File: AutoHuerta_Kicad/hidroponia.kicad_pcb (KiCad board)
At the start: 2 copper layers, 37 parts, among them J1 bornera, J2 bornera, J3 Barrel_Jack, J4 pin, J6 Pin, J7 Pin, K1 RELAY, Q1 BC817, Q2 BS170F, Q3 BC817, U2 PC817, U3 L7805, U4 PC817, U5 L7805, U6 PC817

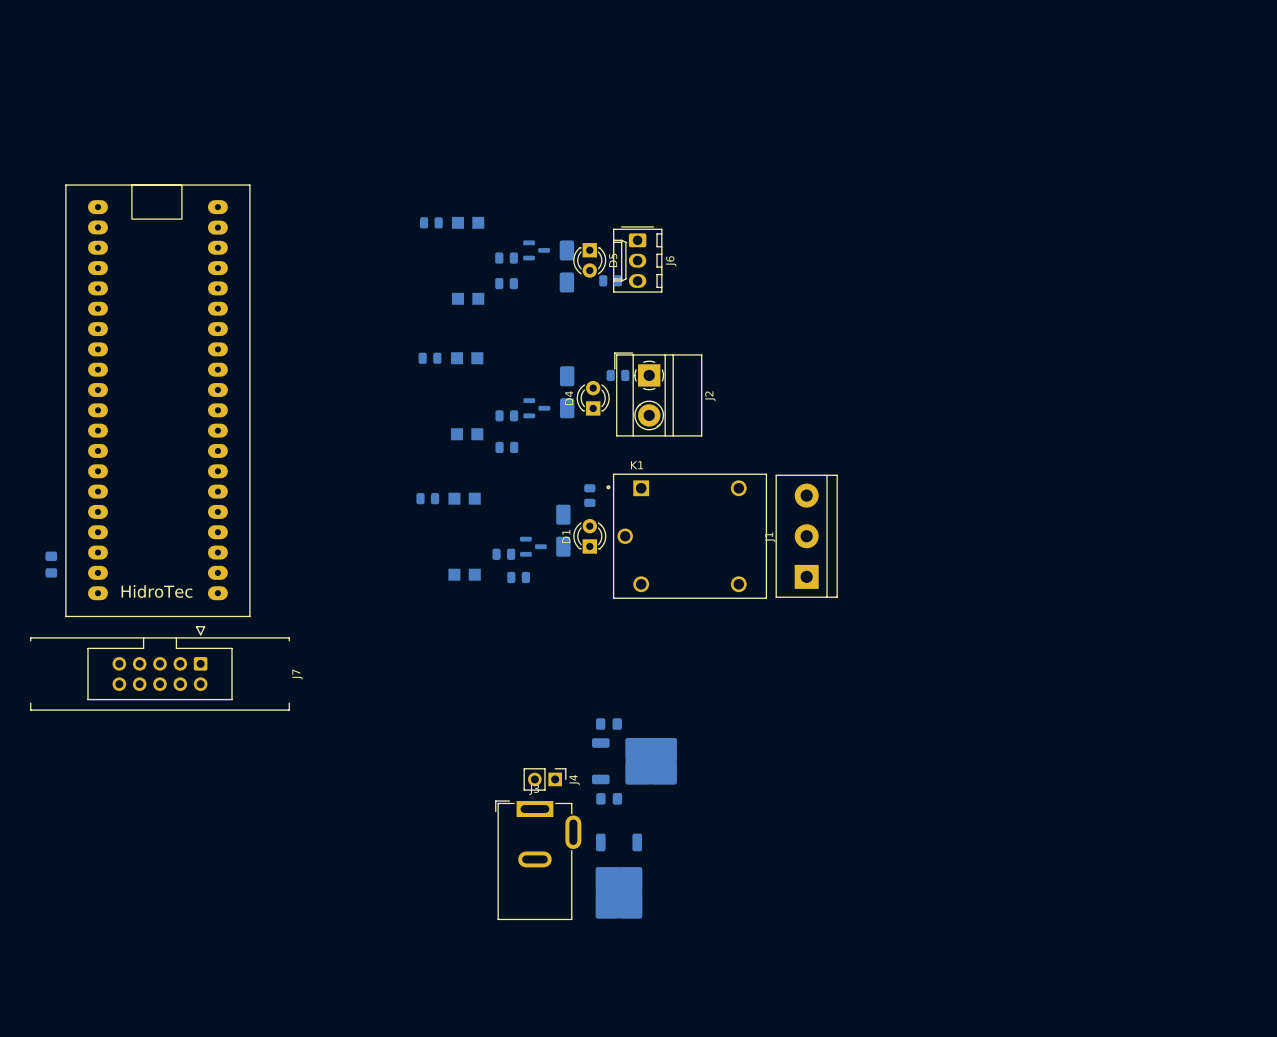
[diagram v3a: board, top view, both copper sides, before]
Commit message: PCB
PCB casi terminado, y cambiamos unas cosas del esquematico
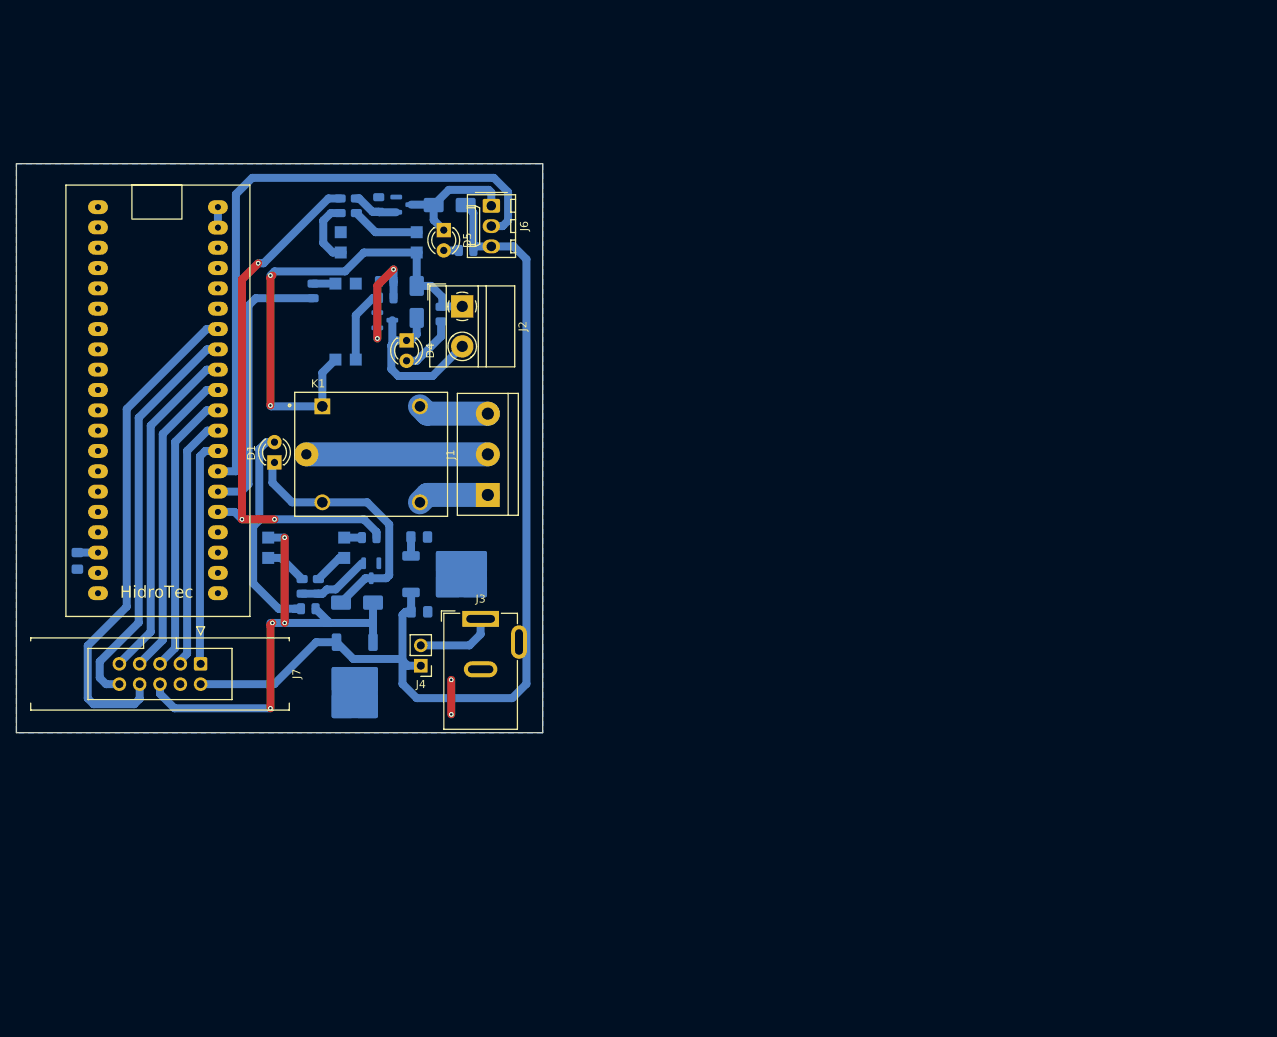
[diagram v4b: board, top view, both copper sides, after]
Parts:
- moved U5 41.4 mm to (77.3, 95.6)
- moved J1 41.2 mm to (94.0, 72.1)
- moved K1 41.2 mm to (79.4, 67.1)
- moved D1 40.8 mm to (67.3, 68.1)
- moved R4 37.9 mm to (71.5, 86.4), turned to 0 degrees
- moved C1 33.3 mm to (85.4, 86.7)
- moved C2 33.3 mm to (85.4, 77.4)
- moved U3 33.3 mm to (89.4, 82.0)
- moved D2 27.3 mm to (77.6, 85.6), turned to 180 degrees
- moved R7 25.6 mm to (81.3, 45.5)
- moved R2 25.5 mm to (70.8, 83.6), turned to -90 degrees
- moved R3 25.0 mm to (72.8, 83.6), turned to -90 degrees
- moved J2 24.9 mm to (90.8, 48.6)
- moved D4 24.8 mm to (83.8, 52.8), turned to -90 degrees
- moved J3 24.7 mm to (93.1, 87.6)
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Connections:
- J3 pad 3: (no net) -> +12V
- J7 pad 1: GND -> A3
- J7 pad 10: B1 -> B0
- J7 pad 3: +5V -> A4
- J7 pad 4: A3 -> GND
- J7 pad 5: A4 -> A5
- J7 pad 6: A5 -> +5V
- J7 pad 8: A7 -> B1
- J7 pad 9: B0 -> A7
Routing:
- net +12V: track 0.00 -> 126.7 mm
- net +5V: track 0.00 -> 120.0 mm, vias 0 -> 6
- net VEL: track 0.00 -> 78.4 mm
- net LED & FAN: track 0.00 -> 68.0 mm, vias 0 -> 3
- net B1: track 0.00 -> 62.6 mm
- net B0: track 0.00 -> 50.8 mm
- net A7: track 0.00 -> 42.7 mm
- net A6: track 0.00 -> 39.1 mm
- net A5: track 0.00 -> 35.5 mm
- net BOMBA: track 0.00 -> 35.0 mm
- net Net-(D1-K): track 0.00 -> 33.1 mm
- net A4: track 0.00 -> 31.9 mm
- net A3: track 0.00 -> 28.5 mm
- net Net-(D1-A): track 0.00 -> 27.3 mm
- net Net-(D3-A): track 0.00 -> 22.8 mm
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- added copper zone on B.Cu, net GND
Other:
- board outline added: 65.8 x 71.1 mm

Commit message: PCB
cambios en el pcb
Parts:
- U2, U4, U6: footprint Package_SO:SSO-4_6.7x5.1mm_P2.54mm_Clearance8mm -> Package_DIP:DIP-4_W7.62mm_LongPads; moved to F.Cu
- moved U5 26.8 mm to (103.8, 91.4), turned to 90 degrees
- moved R4 22.5 mm to (82.6, 66.8)
- moved D5 21.8 mm to (83.4, 60.2), turned to 0 degrees
- moved C2 20.9 mm to (77.0, 96.5), turned to 180 degrees
- moved R11 20.4 mm to (81.5, 56.2), turned to 180 degrees
- moved R10 20.2 mm to (78.1, 56.2), turned to 0 degrees
- moved D6 18.2 mm to (91.3, 54.0), turned to 90 degrees
- moved R9 17.9 mm to (78.9, 53.6), turned to 0 degrees
- moved Q3 17.5 mm to (83.3, 53.4)
- moved D2 17.5 mm to (77.7, 68.1), turned to -90 degrees
- moved R12 16.1 mm to (85.9, 56.8), turned to 90 degrees
- moved J6 16.0 mm to (88.5, 50.9)
- moved U4 16.0 mm to (77.7, 34.6)
- moved K1 14.0 mm to (92.2, 72.8)
- moved J1 14.0 mm to (106.8, 77.9)
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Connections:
- J3 pad 3: +12V -> (no net)
- J6 pad 1: Net-(D5-K) -> VEL
- J6 pad 2: VEL -> Net-(D5-K)
- J7 pad 2: +12V -> +5V
- J7 pad 6: +5V -> +12V
- U1 pad 26: BOMBA -> VEL
- U1 pad 27: VEL -> BOMBA
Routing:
- net +12V: track 126.7 -> 47.3 mm
- net +5V: track 120.0 -> 194.3 mm, vias 6 -> 0
- net +5V1: track 4.97 -> 73.0 mm
- net VEL: track 78.4 -> 46.8 mm
- net LED & FAN: track 68.0 -> 41.3 mm, vias 3 -> 0
- net Net-(D1-A): track 27.3 -> 6.06 mm
- net Net-(D1-K): track 33.1 -> 15.9 mm
- net GND: track 10.5 -> 25.2 mm, vias 2 -> 0
- net Net-(Q2-G): track 14.4 -> 4.38 mm, vias 2 -> 0
- net Net-(D3-A): track 22.8 -> 15.3 mm
- net Net-(R6-Pad1): track 9.47 -> 2.61 mm
- net Net-(R10-Pad1): track 8.79 -> 2.61 mm
- net Net-(R9-Pad2): track 8.23 -> 2.44 mm
- net BOMBA: track 35.0 -> 40.4 mm
- net Net-(Q1-B): track 9.04 -> 4.62 mm
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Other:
- board size 65.8 x 71.1 mm -> 80.6 x 71.1 mm

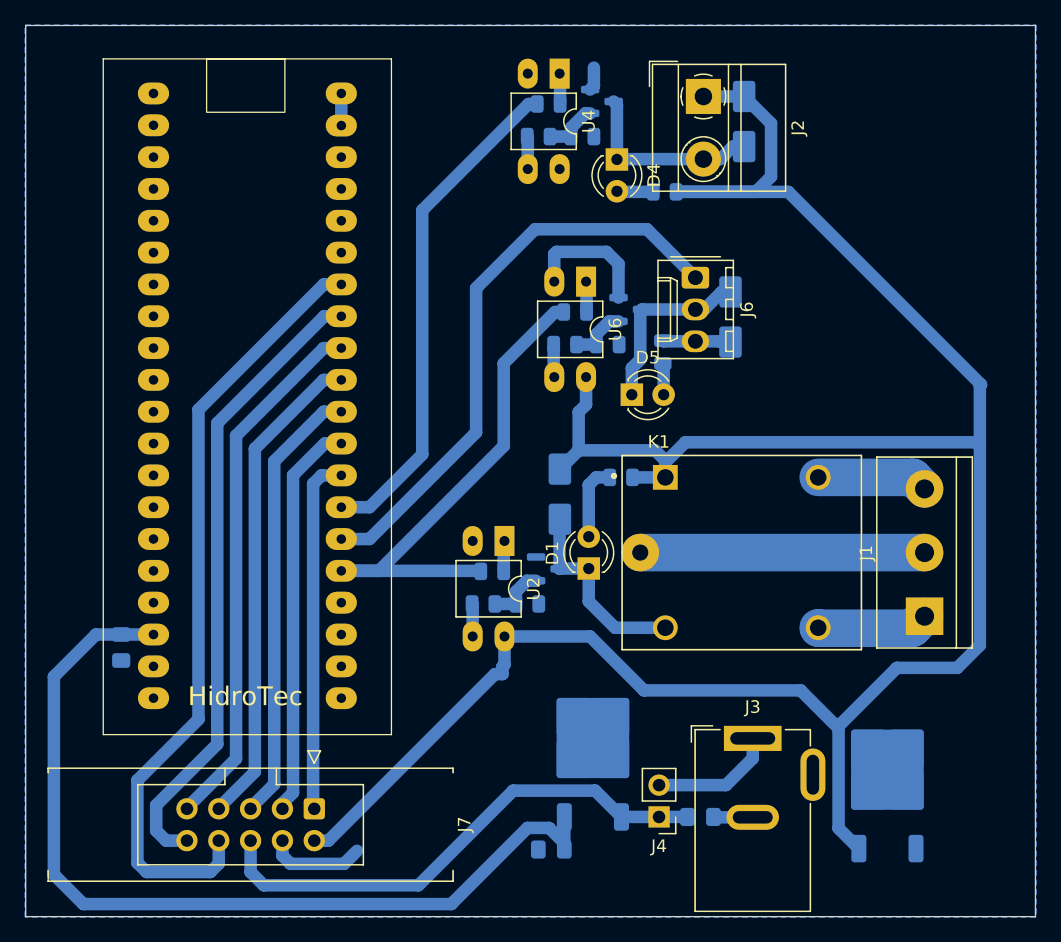
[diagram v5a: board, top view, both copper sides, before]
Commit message: PCB actualizado
faltan enrutar 5 pistas
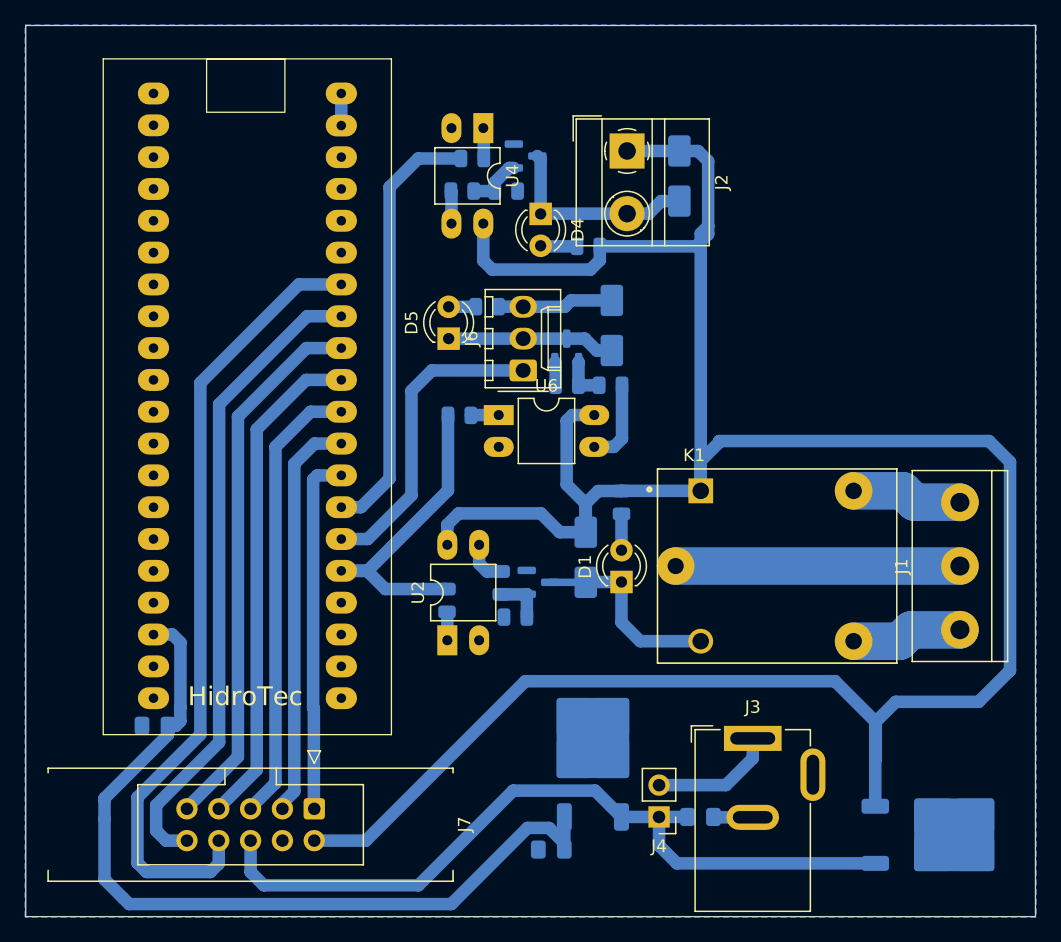
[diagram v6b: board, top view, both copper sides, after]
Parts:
- moved J6 15.6 mm to (74.8, 58.3), turned to 90 degrees
- moved D5 15.3 mm to (68.8, 55.7), turned to 90 degrees
- moved R12 14.5 mm to (71.9, 53.2), turned to 0 degrees
- moved U6 12.7 mm to (72.8, 61.8), turned to 0 degrees
- moved R9 12.4 mm to (69.7, 61.9)
- moved D6 9.49 mm to (81.8, 54.7), turned to -90 degrees
- moved U2 9.14 mm to (68.7, 79.8), turned to 90 degrees
- moved D4 7.48 mm to (76.1, 45.8)
- moved J2 7.48 mm to (83.0, 40.8)
- moved R6 7.48 mm to (69.9, 44.0)
- moved R7 7.48 mm to (73.4, 44.0)
- moved R8 7.48 mm to (80.0, 48.4)
- moved Q2 7.48 mm to (74.9, 41.1)
- moved R5 7.48 mm to (70.7, 41.4)
- moved U4 7.48 mm to (71.6, 38.9)
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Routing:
- net +12V: track 47.3 -> 71.2 mm
- net VEL: track 46.8 -> 25.0 mm
- net GND: track 25.2 -> 6.90 mm
- net +5V: track 194.3 -> 212.2 mm
- net LED & FAN: track 41.3 -> 26.2 mm
- net BOMBA: track 40.4 -> 34.7 mm
- net +5V1: track 73.0 -> 67.8 mm
- net Net-(R10-Pad1): track 2.61 -> 6.75 mm
- net Net-(D1-A): track 6.06 -> 2.90 mm
- net Net-(D5-K): track 14.8 -> 13.4 mm
- net B1: track 62.6 -> 63.8 mm
- net Net-(Q3-B): track 4.59 -> 3.51 mm
- net Net-(D3-A): track 15.3 -> 16.2 mm
- net Net-(R2-Pad1): track 2.61 -> 3.53 mm
- net A6: track 39.1 -> 39.9 mm
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
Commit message: actualizacion de PCB
pruebas
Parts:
- moved C2 2.04 mm to (75.7, 95.0), turned to -90 degrees
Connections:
- J7 pad 2: +5V -> GND
- J7 pad 4: GND -> +5V
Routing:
- net GND: track 6.90 -> 37.2 mm, vias 0 -> 6
- net +5V: track 212.2 -> 217.3 mm
- net +5V1: track 67.8 -> 64.1 mm
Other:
- board size 80.6 x 71.1 mm -> 80.6 x 72.2 mm
